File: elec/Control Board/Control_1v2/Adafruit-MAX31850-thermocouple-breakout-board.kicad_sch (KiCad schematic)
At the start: 48 parts, among them J11 Con_01x02_2.5mm, J2 MAX31850K

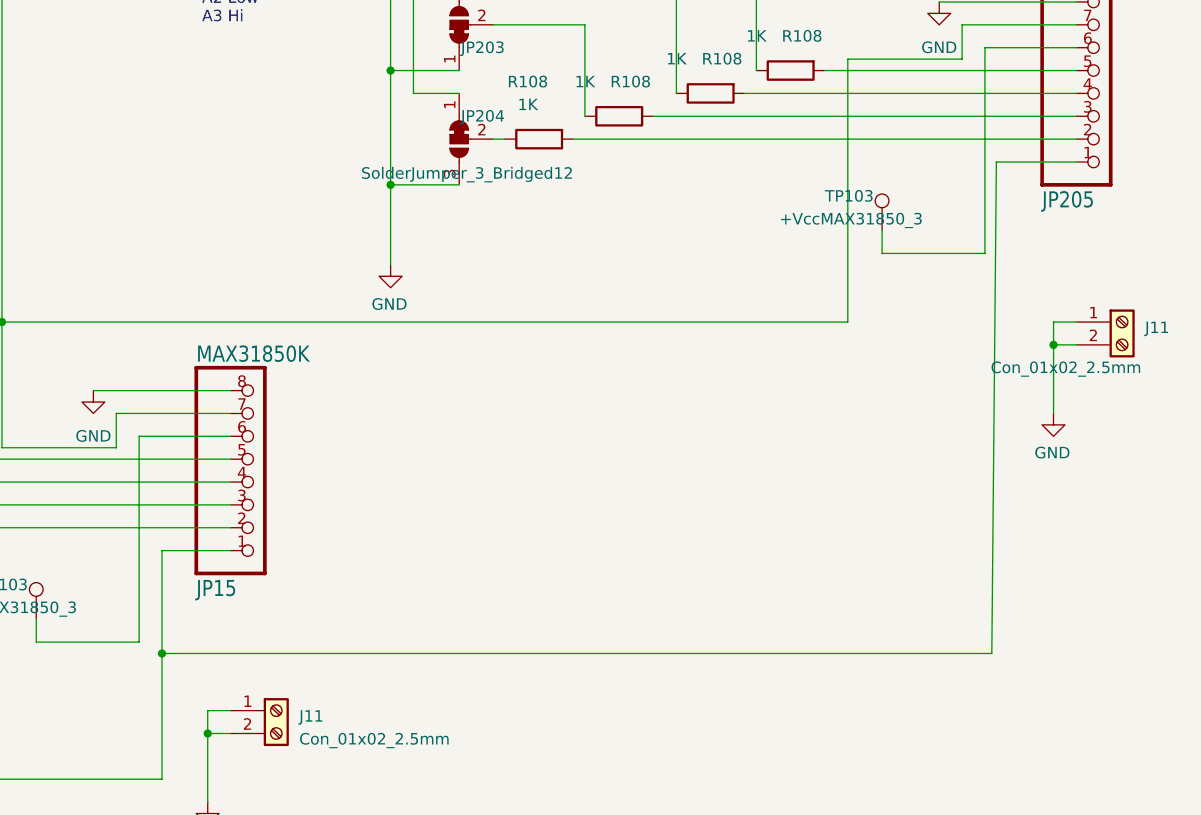
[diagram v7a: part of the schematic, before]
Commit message: Clearing more ERC schematic errors. Only errors related to libraries and ground symbol modified remain.
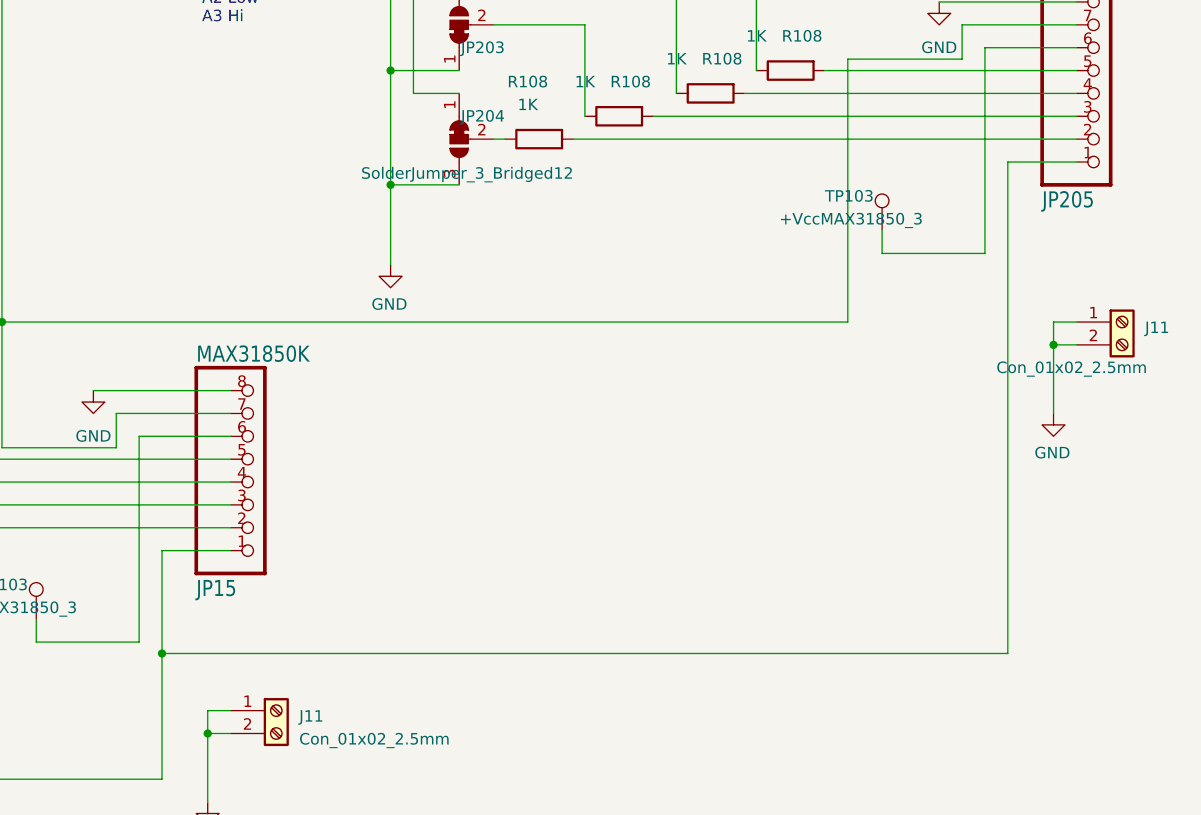
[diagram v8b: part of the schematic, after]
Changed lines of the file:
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@@
     (stroke (width 0) (type default))
   )
-  (wire (pts (xy 397.51 110.49) (xy 406.4 110.49))
+  (wire (pts (xy 398.78 110.49) (xy 406.4 110.49))
     (stroke (width 0) (type default))
   )
@@
     (stroke (width 0) (type default))
   )
-  (wire (pts (xy 397.002 165.1) (xy 397.51 110.49))
+  (wire (pts (xy 398.78 165.1) (xy 398.78 110.49))
     (stroke (width 0) (type default))
   )
-  (wire (pts (xy 304.8 165.1) (xy 397.002 165.1))
+  (wire (pts (xy 304.8 165.1) (xy 398.78 165.1))
     (stroke (width 0) (type default))
   )
@@
       (effects (font (size 1.27 1.27)) (justify left))
     )
-    (property "Value" "Con_01x02_2.5mm" (at 396.875 133.35 0)
+    (property "Value" "Con_01x02_2.5mm" (at 397.51 133.35 0)
       (effects (font (size 1.27 1.27)) (justify left))
     )
